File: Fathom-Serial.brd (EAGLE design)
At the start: 112.4 x 45.7 mm, 115 parts, among them IC1 LMH6643, IC2 LMH6643, IC3 ST490AB, IC4 ST490AB, IC5 FT230XS, Q1 BC817-40W, U1 MC7812, U2 MC7805, U4 INA139, U5 MC7805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

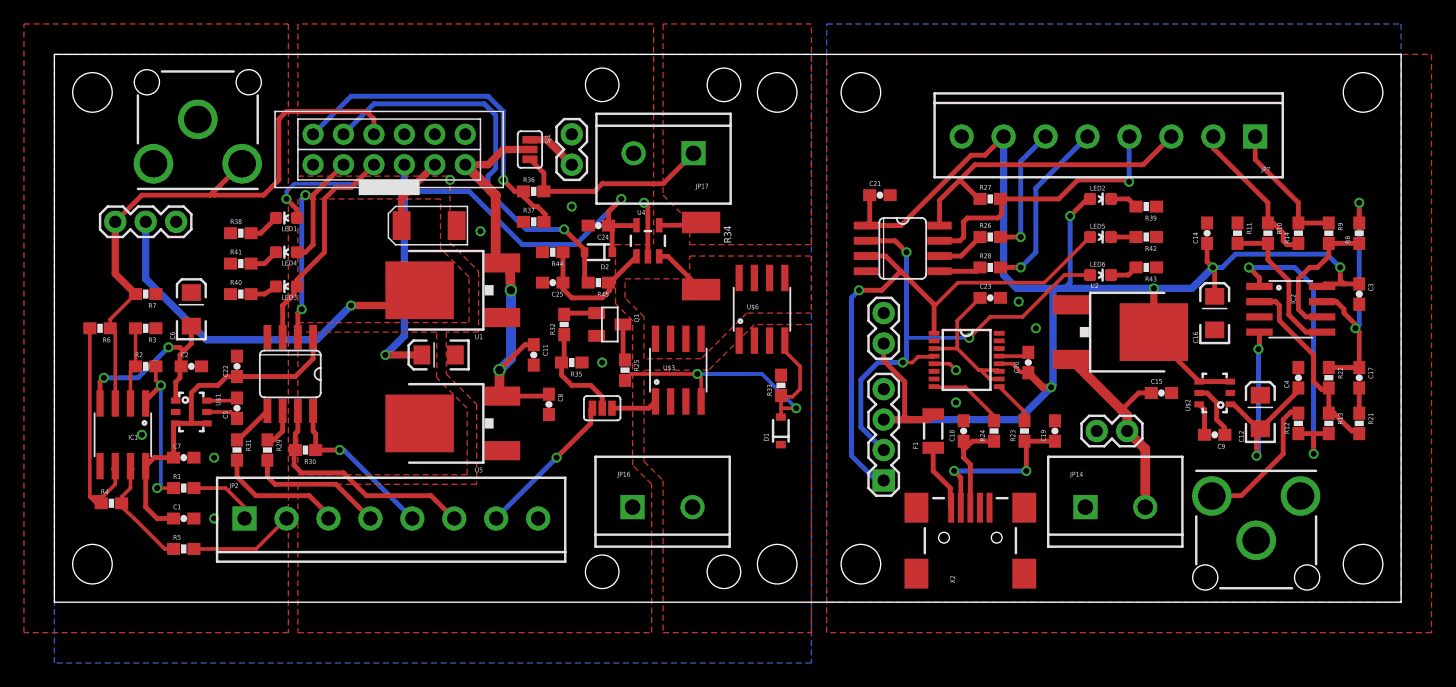
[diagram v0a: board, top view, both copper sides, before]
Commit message: Increased termination resistor size appropriately for RS485. Hopefully we can get by without using these eventually.
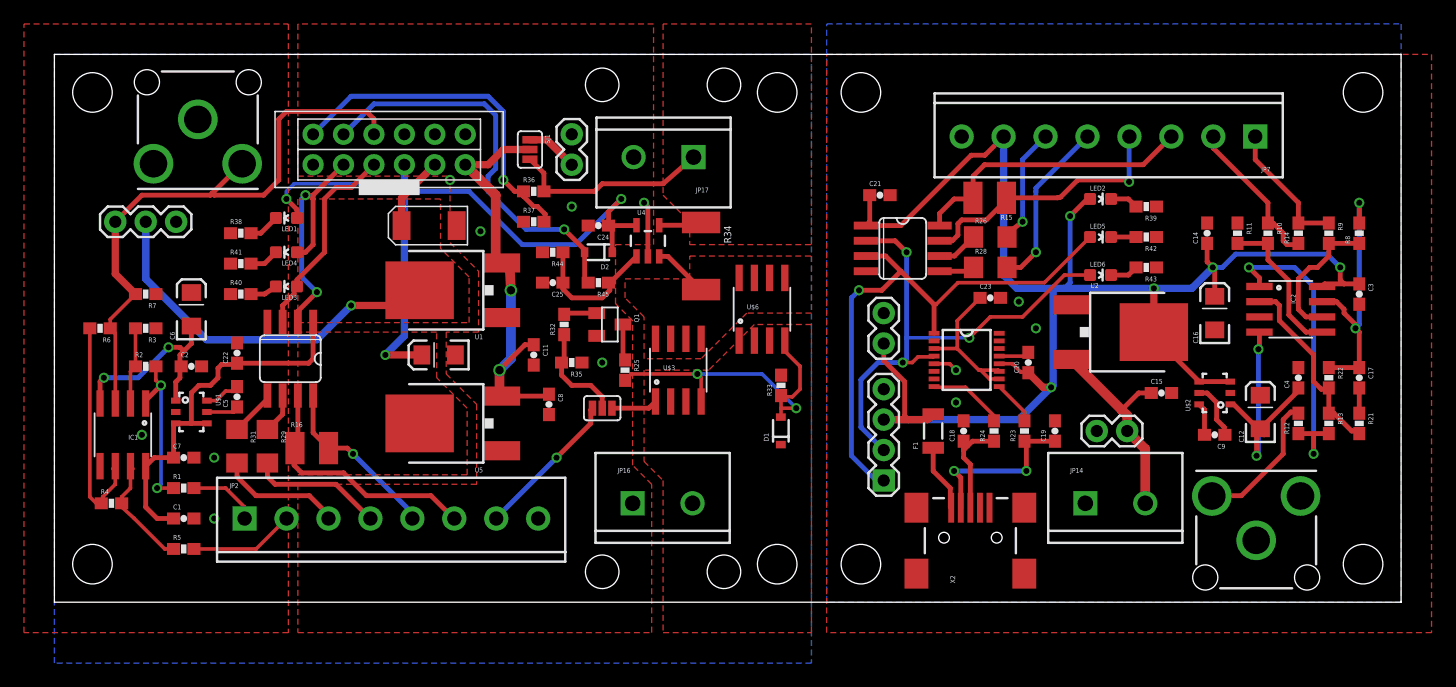
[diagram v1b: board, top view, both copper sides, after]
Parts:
- removed R27, R30: 86.6, SparkFun:0603-RES
- added R15, R16: NP, resistor:R1210
- R26, R28, R29, R31: value 43 -> 0; device SparkFun:0603-RES -> SparkFun:1206
- moved IC4 1.27 mm to (19.7, 20.3)
- moved C22 1.11 mm to (15.2, 20.8)
- moved C5 0.95 mm to (15.2, 17.1)
- moved JP17 0.32 mm to (53.3, 37.1)
- moved JP14 0.32 mm to (86.0, 8.26)
- moved JP16 0.32 mm to (48.3, 8.26)
- moved R29 0.32 mm to (17.8, 13.0)
- moved R31 0.32 mm to (15.2, 13.0)
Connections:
- net ROV-TP3+: now also R16.2; no longer R30.1
- net ROV-TP3-: now also R16.1; no longer R30.2
- net TOP-TP2+: now also R15.2; no longer R27.1
- net TOP-TP2-: now also R15.1; no longer R27.2
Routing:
- net VCC-ISO: track 91.1 -> 92.8 mm
- net ROV-TP3-: track 19.9 -> 21.6 mm
- net ROV-TX: track 18.5 -> 17.2 mm
- net TOP-TP3-: track 10.9 -> 9.83 mm
- net ROV-TP3+: track 13.8 -> 14.6 mm
- net TOP-TP2+: track 26.0 -> 25.3 mm
- net TOP-TP3+: track 14.9 -> 14.4 mm
- net N$26: track 4.04 -> 3.49 mm
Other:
- board text added: "5V OUT"
- board text added: "7-26V IN"
- board text removed: "5V 150mA OUT"
- board text removed: "7-26V"

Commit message: Updated tether ribbon header size and pinout.
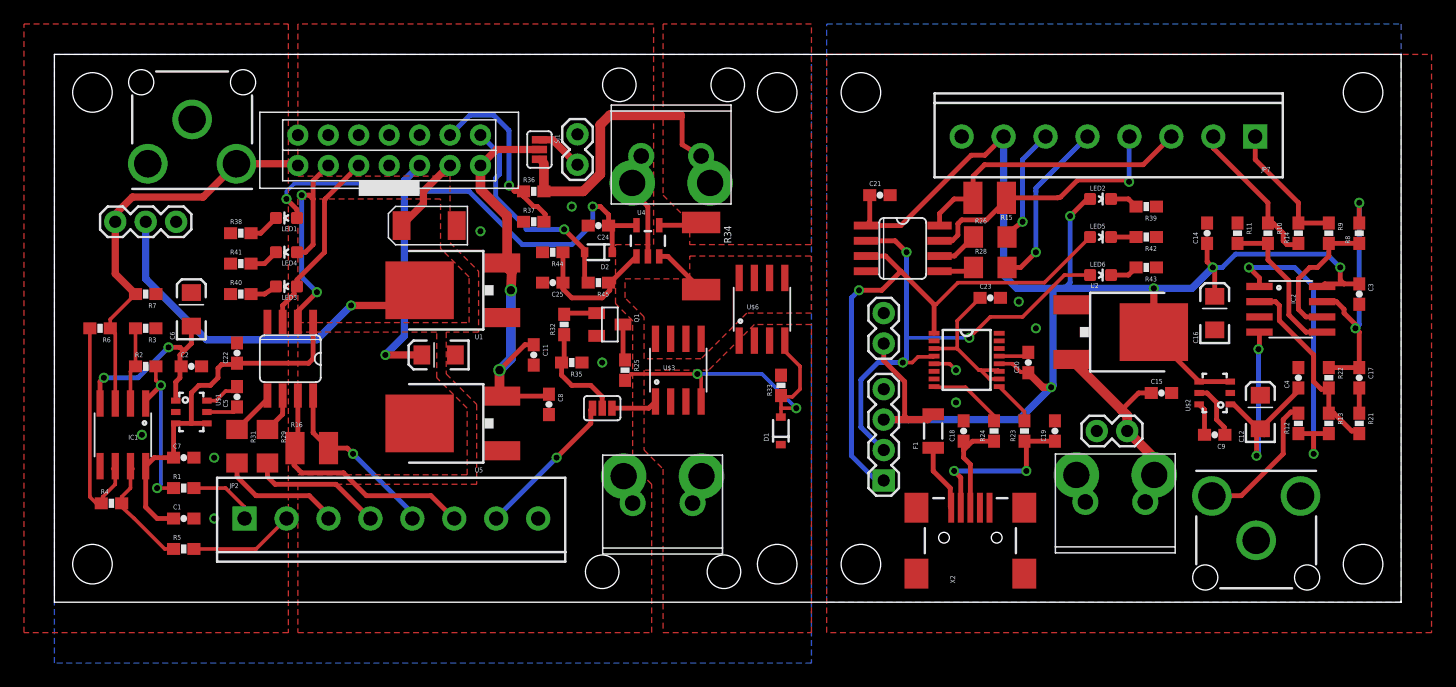
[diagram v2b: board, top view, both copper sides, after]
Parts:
- removed JP14: 1935161, SparkFun-Connectors:SCREWTERMINAL-5MM-2
- removed JP16, JP17: M025MM, SparkFun-Connectors:SCREWTERMINAL-5MM-2
- added U$10, U$11, U$12: HEADER-2, BR-Eagle-Library:TETHER-POWER-TERMINALS
- U$8: device BR-Eagle-Library:TETHER-HEADER-2X6 -> BR-Eagle-Library:TETHER-HEADER-2X7
- moved U$8 1.27 mm to (20.3, 36.4)
- moved SJ1 0.79 mm to (40.5, 37.8)
- moved JP1 0.48 mm to (11.5, 40.3)
- moved JP10 0.48 mm to (43.7, 36.5)
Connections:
- net GND: now also U$12.1A, U$12.1B; no longer JP14.1
- net GND-ISO: now also U$10.1A, U$10.1B, U$11.2A, U$11.2B, U$8.GND0, U$8.GND1, U$8.GND2; no longer JP16.1, JP17.2, U$8.GND-0, U$8.GND-1, U$8.GND-2, U$8.GND-3
- net ROV-BATT: now also U$10.2A, U$10.2B; no longer JP16.2
- net ROV-VIN-SWITCHED: now also U$11.1A, U$11.1B; no longer JP17.1
- net TOP-VIN: now also U$12.2A, U$12.2B; no longer JP14.2
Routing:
- net CAMERA: track 50.5 -> 34.6 mm
- net I_SENSE: track 33.7 -> 18.2 mm
- net V_SENSE: track 29.0 -> 15.7 mm
- net ROV-VIN-SWITCHED: track 20.3 -> 27.2 mm
- net VCC-ISO: track 92.8 -> 91.3 mm
- net ROV-TX: track 17.2 -> 15.9 mm
- net TOP-VIN: track 17.6 -> 18.1 mm
- net GND-ISO: vias 8 -> 6
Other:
- board text added: "NC"
